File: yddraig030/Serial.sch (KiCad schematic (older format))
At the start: 25 parts, among them J1401 Serial1, J1402 Serial2, Q1401 2N4403, Q1402 2N4403, U1401 68681, U1402 MAX202, U1403 MAX202, Y1401 3.6864MHz

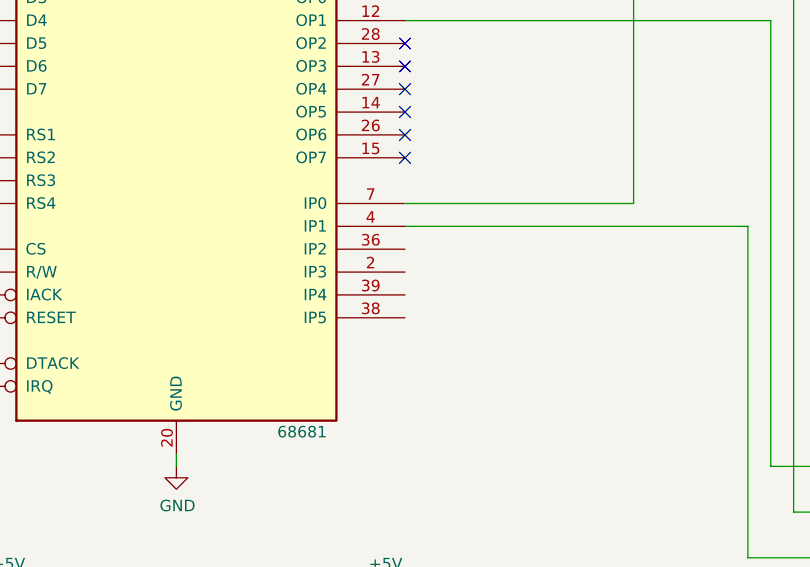
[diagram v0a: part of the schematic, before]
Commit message: ddraig030: trying to fix the DRC errors
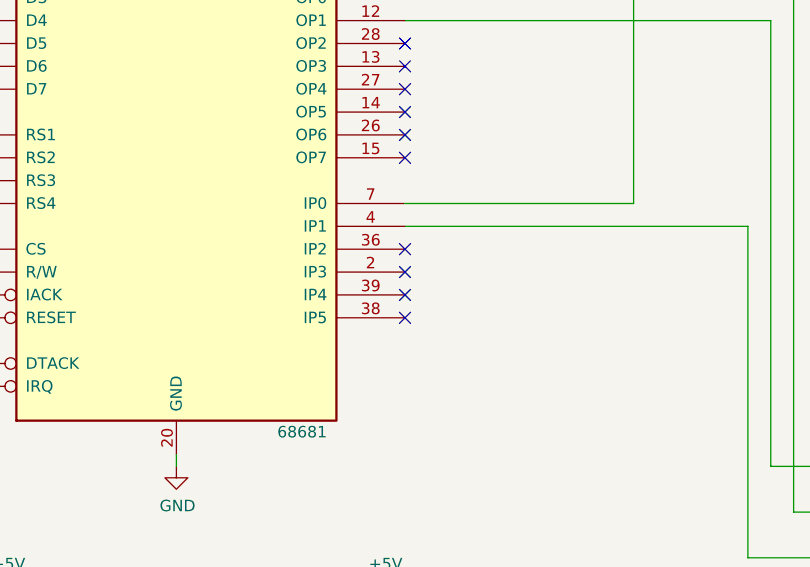
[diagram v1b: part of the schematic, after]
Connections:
- no-connect marks 14 -> 18
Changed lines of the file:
@@
 Wire Wire Line
 	4850 4550 6350 4550
+NoConn ~ 4850 4650
+NoConn ~ 4850 4750
+NoConn ~ 4850 4850
+NoConn ~ 4850 4950
 Wire Bus Line
 	2200 4000 2200 4350
